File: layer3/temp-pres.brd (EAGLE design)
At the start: 16.5 x 12.7 mm, 9 parts, among them U1 TMP1021:1, U2 MS5803-14BA

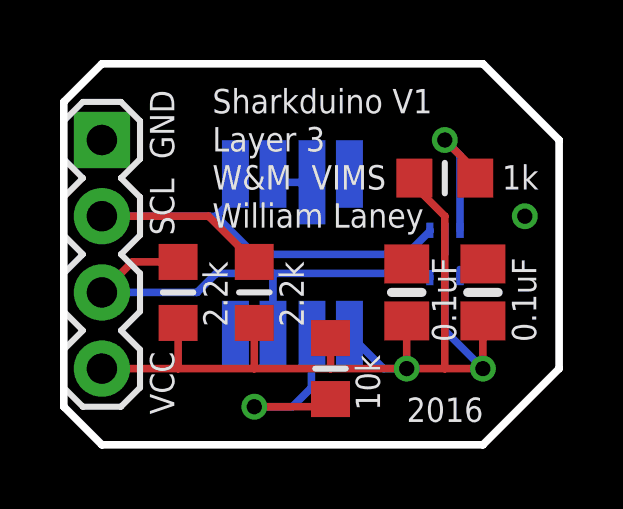
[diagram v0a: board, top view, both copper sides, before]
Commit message: tweaked layer3 silk screen for printing
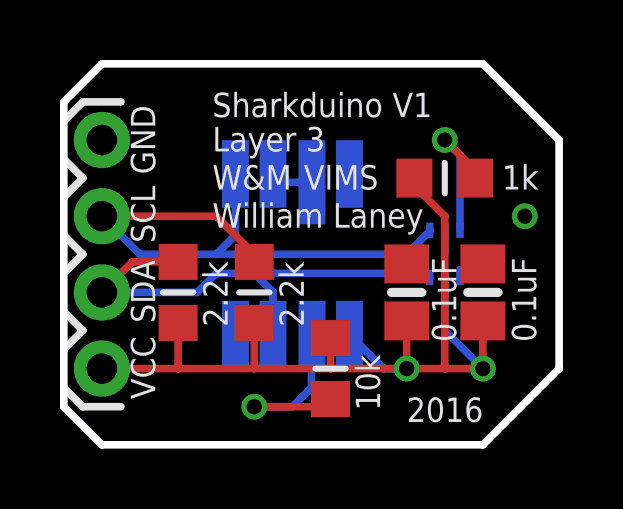
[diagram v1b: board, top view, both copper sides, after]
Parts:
- removed J1: (no value), SparkFun-Connectors:1X04
- added J2: (no value), SparkFun-Connectors:1X04_NO_SILK_ALL_ROUND
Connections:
- net +3V3: now also J2.4; no longer J1.4
- net GND: now also J2.1; no longer J1.1
- net SCL: now also J2.2; no longer J1.2
- net SDA: now also J2.3; no longer J1.3
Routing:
- net SCL: track 19.2 -> 20.6 mm
